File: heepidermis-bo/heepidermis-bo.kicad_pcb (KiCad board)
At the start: 4 copper layers, 85.7 x 54 mm, 10 parts, among them J2 PinHeader_2x16_P1.27mm_Vertic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, J3 PinHeader_2x16_P1.27mm_Vertic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

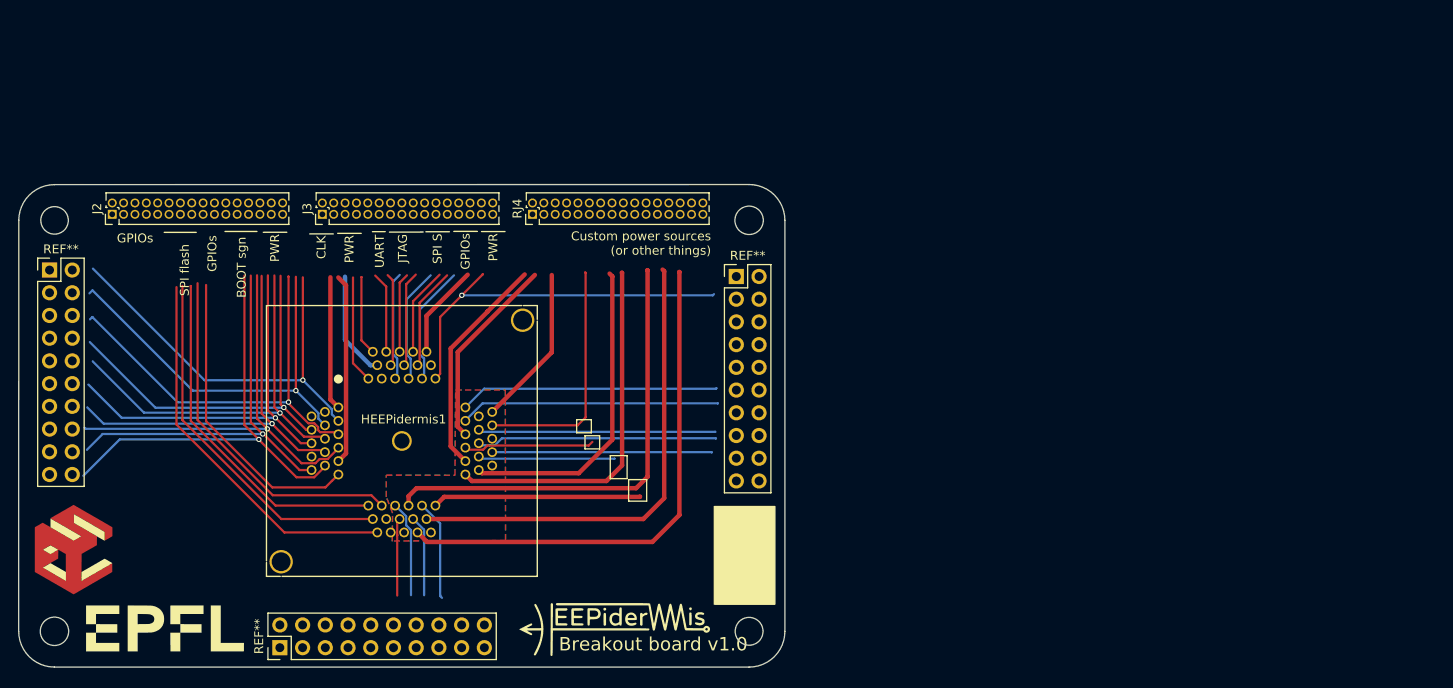
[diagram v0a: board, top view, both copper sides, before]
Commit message: Previous to changing connector to 2.54
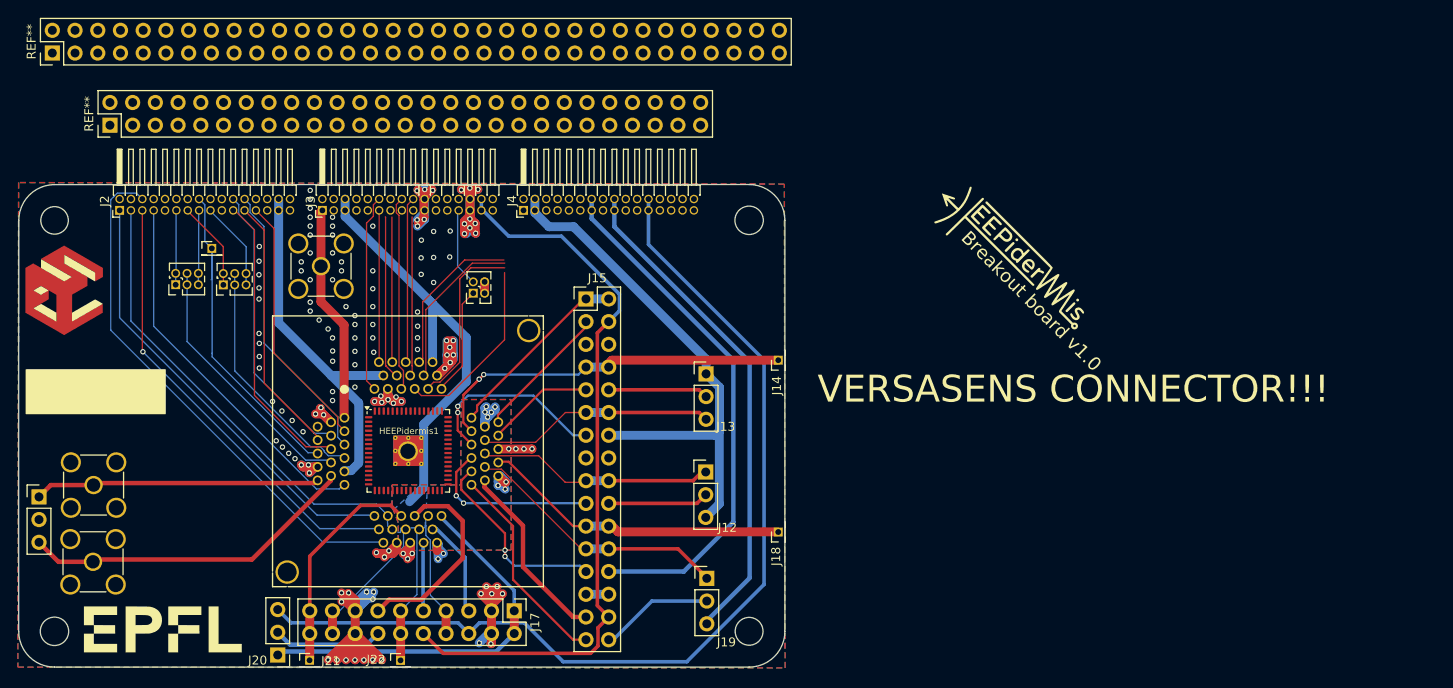
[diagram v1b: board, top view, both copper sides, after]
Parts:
- removed the REF** at (96.9, 80.4)
- removed the REF** at (173.6, 81.1)
- removed the REF** at (122.6, 122.6)
- removed RJ4: PinHeader_2x16_P1.27mm_Vertical, Connector_PinHeader_1.27mm:PinHeader_2x16_P1.27mm_Vertical
- added G***: LOGO, LOGO, B.Cu at (113.5, 106.6)
- added G***: LOGO, LOGO, B.Cu at (113.3, 116.1)
- added G***: LOGO, LOGO, B.Cu at (113.2, 95.5)
- added G***: LOGO, LOGO, B.Cu at (115.0, 86.9)
- added J1: Conn_01x03, Connector_PinHeader_1.27mm:PinHeader_1x01_P1.27mm_Vertical, F.Cu at (115.0, 78.0)
- added J10: Conn_Boaxial, Connector_Coaxial:SMA_Amphenol_901-144_Vertical, F.Cu at (101.8, 104.5)
- added J11: Conn_Boaxial, Connector_Coaxial:SMA_Amphenol_901-144_Vertical, F.Cu at (127.2, 80.0)
- added J12: Conn_01x03, Connector_PinHeader_2.54mm:PinHeader_1x03_P2.54mm_Vertical, F.Cu at (170.2, 103.0)
- added J13: Conn_01x03, Connector_PinHeader_2.54mm:PinHeader_1x03_P2.54mm_Vertical, F.Cu at (170.3, 92.0)
- added J14: Conn_01x03, Connector_PinHeader_1.27mm:PinHeader_1x01_P1.27mm_Vertical, F.Cu at (178.3, 90.5)
- added J15: Conn_02x16_Odd_Even, Connector_PinHeader_2.54mm:PinHeader_2x16_P2.54mm_Vertical, F.Cu at (156.8, 83.6)
- added J17: Conn_02x10_Odd_Even, Connector_PinHeader_2.54mm:PinHeader_2x10_P2.54mm_Vertical, F.Cu at (148.8, 118.5)
- added J18: Conn_01x03, Connector_PinHeader_1.27mm:PinHeader_1x01_P1.27mm_Vertical, F.Cu at (178.3, 109.7)
- added J19: Conn_01x03, Connector_PinHeader_2.54mm:PinHeader_1x03_P2.54mm_Vertical, F.Cu at (170.3, 114.9)
- added J20: Conn_01x03, Connector_PinHeader_2.54mm:PinHeader_1x03_P2.54mm_Vertical, F.Cu at (122.4, 123.5)
- added J21: Conn_01x03, Connector_PinHeader_1.27mm:PinHeader_1x01_P1.27mm_Vertical, F.Cu at (125.9, 124.0)
- added J22: Conn_01x03, Connector_PinHeader_1.27mm:PinHeader_1x01_P1.27mm_Vertical, F.Cu at (136.1, 124.0)
- added J4: Conn_02x16_Odd_Even, Connector_PinHeader_1.27mm:PinHeader_2x16_P1.27mm_Horizontal, F.Cu at (149.8, 73.7)
- added J5: Conn_01x03, Connector_PinHeader_1.27mm:PinHeader_2x03_P1.27mm_Vertical, F.Cu at (116.3, 82.1)
- added J6: Conn_01x03, Connector_PinHeader_1.27mm:PinHeader_2x03_P1.27mm_Vertical, F.Cu at (111.0, 82.0)
- added J7: Conn_01x03, Connector_PinHeader_2.54mm:PinHeader_1x03_P2.54mm_Vertical, F.Cu at (95.7, 105.8)
- added J8: Conn_01x03, Connector_PinHeader_1.27mm:PinHeader_2x02_P1.27mm_Vertical, F.Cu at (144.2, 83.0)
- added J9: Conn_Boaxial, Connector_Coaxial:SMA_Amphenol_901-144_Vertical, F.Cu at (101.7, 113.0)
- added REF**: PinHeader_2x27_P2.54mm_Vertical, Connector_PinHeader_2.54mm:PinHeader_2x27_P2.54mm_Vertical, F.Cu at (103.6, 64.2)
- added REF**: PinHeader_2x33_P2.54mm_Vertical, Connector_PinHeader_2.54mm:PinHeader_2x33_P2.54mm_Vertical, F.Cu at (97.2, 56.1)
- added REF**: QFN-64-1EP_9x9mm_P0.5mm_EP3.4x3.4mm_ThermalVias, Package_DFN_QFN:QFN-64-1EP_9x9mm_P0.5mm_EP3.4x3.4mm_ThermalVias, F.Cu at (137.0, 100.6)
- J2, J3: value PinHeader_2x16_P1.27mm_Vertical -> Conn_02x16_Odd_Even; footprint Connector_PinHeader_1.27mm:PinHeader_2x16_P1.27mm_Vertical -> Connector_PinHeader_1.27mm:PinHeader_2x16_P1.27mm_Horizontal
- moved G*** 60.6 mm to (204.2, 79.0), turned to -45 degrees
- moved REF** 29.0 mm to (98.6, 87.6)
- moved HEEPidermis1 1.34 mm to (129.8, 96.9)
- moved J2 0.93 mm to (104.7, 73.7)
- moved J3 0.44 mm to (127.4, 73.7)
- moved REF** 0.26 mm to (110.1, 120.6)
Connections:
- HEEPidermis1 pad 1: /CLK -> /CLOCK
- HEEPidermis1 pad 12: /VSS -> /ACORE_VSS
- HEEPidermis1 pad 16: /SPI_FLASH_CS_1 -> /SPI_FLASH.CS1
- HEEPidermis1 pad 17: /SPI_FLASH_SD_1 -> /SPI_FLASH.SD1
- HEEPidermis1 pad 18: /SPI_FLASH_SD_0 -> /SPI_FLASH.SD0
- HEEPidermis1 pad 19: /SPI_FLASH_SCK -> /SPI_FLASH.SCK
- HEEPidermis1 pad 2: /VSS -> /ACORE_VSS
- HEEPidermis1 pad 20: /SPI_FLASH_CS_0 -> /SPI_FLASH.CS0
- HEEPidermis1 pad 22: /VSS -> /ACORE_VSS
- HEEPidermis1 pad 50: /VSS -> /ACORE_VSS
- HEEPidermis1 pad 56: /JTAG_TRST -> /JTAG.TRST
- HEEPidermis1 pad 57: /JTAG_TMS -> /JTAG.TMS
- HEEPidermis1 pad 58: /JTAG_TDI -> /JTAG.TDI
- HEEPidermis1 pad 59: /JTAG_TCK -> /JTAG.TCK
- HEEPidermis1 pad 60: /JTAG_TDO -> /JTAG.TDO
- HEEPidermis1 pad 61: /VSS -> /ACORE_VSS
- HEEPidermis1 pad 63: /UART_TX -> /UART.TX
- HEEPidermis1 pad 64: /UART_RX -> /UART.RX
- HEEPidermis1 pad 9: /VCO_CNT_OVF -> /GPIO_5
- J2 pad 1: (no net) -> /SPI_FLASH.SD1
- J2 pad 10: (no net) -> /ACORE_VSS
- J2 pad 11: (no net) -> /GPIO_8
- J2 pad 12: (no net) -> /GPIO_9
- J2 pad 13: (no net) -> /GPIO_6
- J2 pad 14: (no net) -> /GPIO_7
- J2 pad 15: (no net) -> /GPIO.LED_B_1
- J2 pad 16: (no net) -> /GPIO_5
- J2 pad 17: (no net) -> /GPIO.LED_R_1
- J2 pad 18: (no net) -> /GPIO.LED_G_1
- J2 pad 19: (no net) -> /ACORE_VSS
- J2 pad 2: (no net) -> /SPI_FLASH.SD2
- J2 pad 20: (no net) -> /ACORE_VSS
- J2 pad 21: (no net) -> /BOOT_SEL
- J2 pad 22: (no net) -> /EXEC_FLASH
- J2 pad 23: (no net) -> /EXIT_VALID
- J2 pad 24: (no net) -> /EXIT_VALUE
- J2 pad 25: (no net) -> /nRST
- J2 pad 26: (no net) -> unconnected-(J2-Pin_26-Pad26)
- J2 pad 27: (no net) -> /ACORE_VSS
- J2 pad 28: (no net) -> /ACORE_VSS
- J2 pad 29: (no net) -> /IO_VDD
- J2 pad 3: (no net) -> /SPI_FLASH.CS0
- J2 pad 30: (no net) -> /IO_VDD
- J2 pad 31: (no net) -> /Vout_B_4
- J2 pad 32: (no net) -> /Vout_diff_4
- J2 pad 4: (no net) -> /SPI_FLASH.SD3
- J2 pad 5: (no net) -> /SPI_FLASH.SD0
- J2 pad 6: (no net) -> /SPI_FLASH.SCK
- J2 pad 7: (no net) -> /SPI_FLASH.CS1
- J2 pad 8: (no net) -> unconnected-(J2-Pin_8-Pad8)
- J2 pad 9: (no net) -> /ACORE_VSS
- J3 pad 1: (no net) -> /CLOCK
- J3 pad 10: (no net) -> /ACORE_VSS
- J3 pad 11: (no net) -> /UART.TX
- J3 pad 12: (no net) -> /UART.RX
- J3 pad 13: (no net) -> /JTAG.TRST
- J3 pad 14: (no net) -> /ACORE_VSS
- J3 pad 15: (no net) -> /JTAG.TDO
- J3 pad 16: (no net) -> /JTAG.TDI
- J3 pad 17: (no net) -> /JTAG.TCK
- J3 pad 18: (no net) -> /JTAG.TMS
- J3 pad 19: (no net) -> /ACORE_VSS
- J3 pad 2: (no net) -> /ACORE_VSS
- J3 pad 20: (no net) -> /ACORE_VSS
- J3 pad 21: (no net) -> /SPI_S_MOSI
- J3 pad 22: (no net) -> /SPI_S_MISO
- J3 pad 23: (no net) -> /SPI_S_CS
- J3 pad 24: (no net) -> /SPI_S_SCK
- J3 pad 25: (no net) -> /GPIO.LED_R_2
- J3 pad 26: (no net) -> /GPIO.LED_G_2
- J3 pad 27: (no net) -> /ACORE_VSS
- J3 pad 28: (no net) -> /ACORE_VSS
- J3 pad 29: (no net) -> /Vout_A_6
- J3 pad 3: (no net) -> /ACORE_VSS
- J3 pad 30: (no net) -> /Vout_A_6
- J3 pad 31: (no net) -> /Vout_B_6
- J3 pad 32: (no net) -> /Vout_diff_6
- J3 pad 4: (no net) -> /ACORE_VSS
- J3 pad 5: (no net) -> /DCORE_VDD
- J3 pad 6: (no net) -> /DCORE_VDD
- J3 pad 7: (no net) -> /Vout_B_5
- J3 pad 8: (no net) -> /Vout_diff_5
- J3 pad 9: (no net) -> /ACORE_VSS
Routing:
- net /ACORE_VSS: track 0.00 -> 170.6 mm, vias 0 -> 142
- net /Vout_A_11: track 0.00 -> 109.2 mm
- net /Vout_A_6: track 0.00 -> 82.6 mm
- net /Vout_A_7: track 0.00 -> 59.5 mm
- net /SPI_FLASH.SCK: track 0.00 -> 59.0 mm
- net /Vout_A_9: track 0.00 -> 58.9 mm
- net /Vout_A_10: track 0.00 -> 55.7 mm
- net /VCO_VN0_VDD: track 58.1 -> 7.71 mm
- net /SPI_FLASH.SD0: track 0.00 -> 50.4 mm, vias 0 -> 1
- net /SPI_FLASH.CS0: track 0.00 -> 50.0 mm
- net /SPI_FLASH.SD1: track 0.00 -> 49.6 mm
- net /VCO_CNT_OVF: track 43.9 -> 0.00 mm, vias 1 -> 0
- net /SPI_FLASH_SCK: track 42.8 -> 0.00 mm
- net /LDO_VBAT: track 53.2 -> 11.2 mm
- net /SPI_FLASH.CS1: track 0.00 -> 42.0 mm
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- added copper zone on B.Cu, net /DCORE_VDD
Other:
- board text added: "VERSASENS CONNECTOR!!!"
- board text removed: "BOOT sgn"
- board text removed: "CLK"
- board text removed: "Custom power sources (or other things)"
- board text removed: "GPIOs"
- board text removed: "JTAG"
- board text removed: "PWR"
- board text removed: "SPI S"
- board text removed: "SPI flash"
- board text removed: "UART"
